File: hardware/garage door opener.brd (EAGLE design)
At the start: 50.8 x 40.6 mm, 26 parts, among them K1 HE3621, K2 HE3621

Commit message: Updated with BOM
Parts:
- C1, C2: value (none) -> 10uf
- D1, D2: value (none) -> 1N4004
- R1, R3: value (none) -> 20
- R2, R4: value 2.3k -> 4k
- R5, R6: value (none) -> 1k
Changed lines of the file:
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@@
 </autorouter>
 <elements>
-<element name="T1" library="transistor-neu-to92" package="SOT23-BEC" value="" x="21.59" y="5.08"/>
+<element name="T1" library="transistor-neu-to92" package="SOT23-BEC" value="" x="21.59" y="5.08">
+<attribute name="MPN" value="MMBT2222A" x="21.59" y="5.08" size="1.778" layer="27" display="off"/>
+</element>
 <element name="K1" library="relay" package="HE3621" value="HE3621" x="40.64" y="10.16" rot="R90">
 <attribute name="OC_NEWARK" value="50F7993" x="40.64" y="10.16" size="1.778" layer="27" rot="R90" display="off"/>
@@
 <element name="JP2" library="pinhead" package="1X15" value="" x="12.7" y="20.32" rot="R270"/>
 <element name="JP3" library="pinhead" package="1X15" value="" x="35.56" y="20.32" rot="R270"/>
-<element name="OPEN1" library="adafruit" package="1X2-3.5MM" value="1X2-3.5MM" x="48.26" y="8.89" rot="R90"/>
-<element name="SENS1" library="adafruit" package="1X2-3.5MM" value="1X2-3.5MM" x="48.26" y="16.51" rot="R90"/>
-<element name="R1" library="resistor" package="R0603" value="" x="44.45" y="2.54" rot="R270"/>
-<element name="R2" library="resistor" package="R0603" value="2.3k" x="17.78" y="5.08" rot="R270"/>
-<element name="D1" library="diode" package="DO214BA" value="" x="26.67" y="5.08" rot="R90"/>
-<element name="C1" library="resistor" package="C0603" value="" x="2.54" y="6.35"/>
-<element name="C2" library="resistor" package="C0603" value="" x="2.54" y="10.16"/>
+<element name="OPEN1" library="adafruit" package="1X2-3.5MM" value="1X2-3.5MM" x="48.26" y="8.89" rot="R90">
+<attribute name="MPN" value="OSTTE020161" x="48.26" y="8.89" size="1.778" layer="27" rot="R90" display="off"/>
+</element>
+<element name="SENS1" library="adafruit" package="1X2-3.5MM" value="1X2-3.5MM" x="48.26" y="16.51" rot="R90">
+<attribute name="MPN" value="OSTTE020161" x="48.26" y="16.51" size="1.778" layer="27" rot="R90" display="off"/>
+</element>
+<element name="R1" library="resistor" package="R0603" value="20" x="44.45" y="2.54" rot="R270"/>
+<element name="R2" library="resistor" package="R0603" value="4k" x="17.78" y="5.08" rot="R270"/>
+<element name="D1" library="diode" package="DO214BA" value="1N4004" x="26.67" y="5.08" rot="R90"/>
+<element name="C1" library="resistor" package="C0603" value="10uf" x="2.54" y="6.35"/>
+<element name="C2" library="resistor" package="C0603" value="10uf" x="2.54" y="10.16"/>
 <element name="LED1" library="resistor" package="R0603" value="" x="1.905" y="33.02" rot="R90"/>
 <element name="LED2" library="resistor" package="R0603" value="" x="1.905" y="26.67" rot="R90"/>
-<element name="SENS2" library="adafruit" package="1X2-3.5MM" value="1X2-3.5MM" x="48.26" y="31.75" rot="R90"/>
-<element name="R3" library="resistor" package="R0603" value="" x="44.45" y="38.1" rot="R270"/>
+<element name="SENS2" library="adafruit" package="1X2-3.5MM" value="1X2-3.5MM" x="48.26" y="31.75" rot="R90">
+<attribute name="MPN" value="OSTTE020161" x="48.26" y="31.75" size="1.778" layer="27" rot="R90" display="off"/>
+</element>
+<element name="R3" library="resistor" package="R0603" value="20" x="44.45" y="38.1" rot="R270"/>
 <element name="K2" library="relay" package="HE3621" value="HE3621" x="40.64" y="30.48" rot="R90">
 <attribute name="OC_NEWARK" value="50F7993" x="40.64" y="30.48" size="1.778" layer="27" rot="R90" display="off"/>
@@
 <attribute name="OC_FARNELL" value="9561943" x="40.64" y="30.48" size="1.778" layer="27" rot="R90" display="off"/>
 </element>
-<element name="OPEN2" library="adafruit" package="1X2-3.5MM" value="1X2-3.5MM" x="48.26" y="24.13" rot="R90"/>
-<element name="T2" library="transistor-neu-to92" package="SOT23-BEC" value="" x="21.59" y="29.21"/>
-<element name="D2" library="diode" package="DO214BA" value="" x="26.67" y="29.21" rot="R90"/>
-<element name="R4" library="resistor" package="R0603" value="2.3k" x="17.78" y="29.21" rot="R270"/>
+<element name="OPEN2" library="adafruit" package="1X2-3.5MM" value="1X2-3.5MM" x="48.26" y="24.13" rot="R90">
+<attribute name="MPN" value="OSTTE020161" x="48.26" y="24.13" size="1.778" layer="27" rot="R90" display="off"/>
+</element>
+<element name="T2" library="transistor-neu-to92" package="SOT23-BEC" value="" x="21.59" y="29.21">
+<attribute name="MPN" value="MMBT2222A" x="21.59" y="29.21" size="1.778" layer="27" display="off"/>
+</element>
+<element name="D2" library="diode" package="DO214BA" value="1N4004" x="26.67" y="29.21" rot="R90"/>
+<element name="R4" library="resistor" package="R0603" value="4k" x="17.78" y="29.21" rot="R270"/>
 <element name="JP4" library="pinhead" package="1X03" value="" x="2.54" y="20.32" rot="R270"/>
 <element name="D3" library="diode" package="DO41-10" value="1N4004" x="30.48" y="7.62" rot="R90"/>
 <element name="D4" library="diode" package="DO41-10" value="1N4004" x="30.48" y="31.75" rot="R90"/>
-<element name="R5" library="resistor" package="R0603" value="" x="4.445" y="33.02" rot="R270"/>
-<element name="R6" library="resistor" package="R0603" value="" x="4.445" y="26.67" rot="R270"/>
+<element name="R5" library="resistor" package="R0603" value="1k" x="4.445" y="33.02" rot="R270"/>
+<element name="R6" library="resistor" package="R0603" value="1k" x="4.445" y="26.67" rot="R270"/>
 </elements>
 <signals>

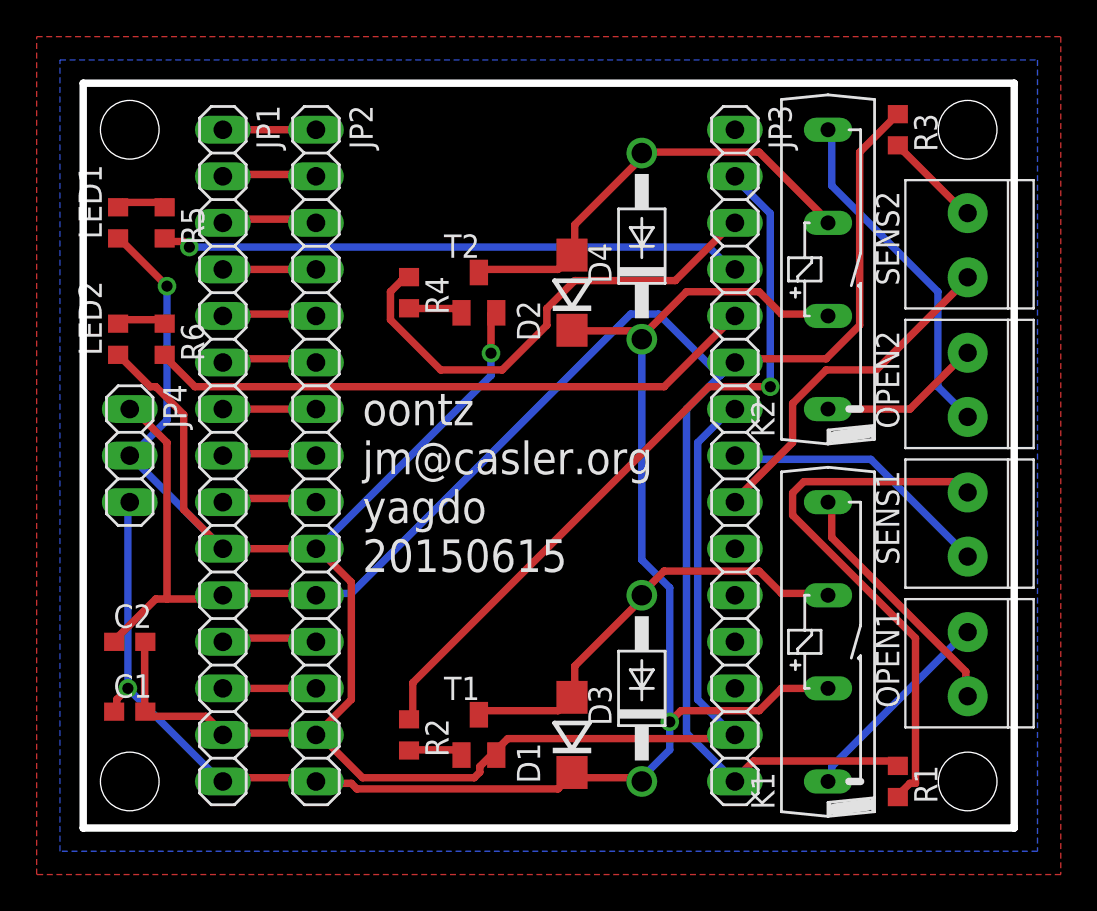
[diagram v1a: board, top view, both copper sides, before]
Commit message: Updated with pull down resistor for sense inputs.
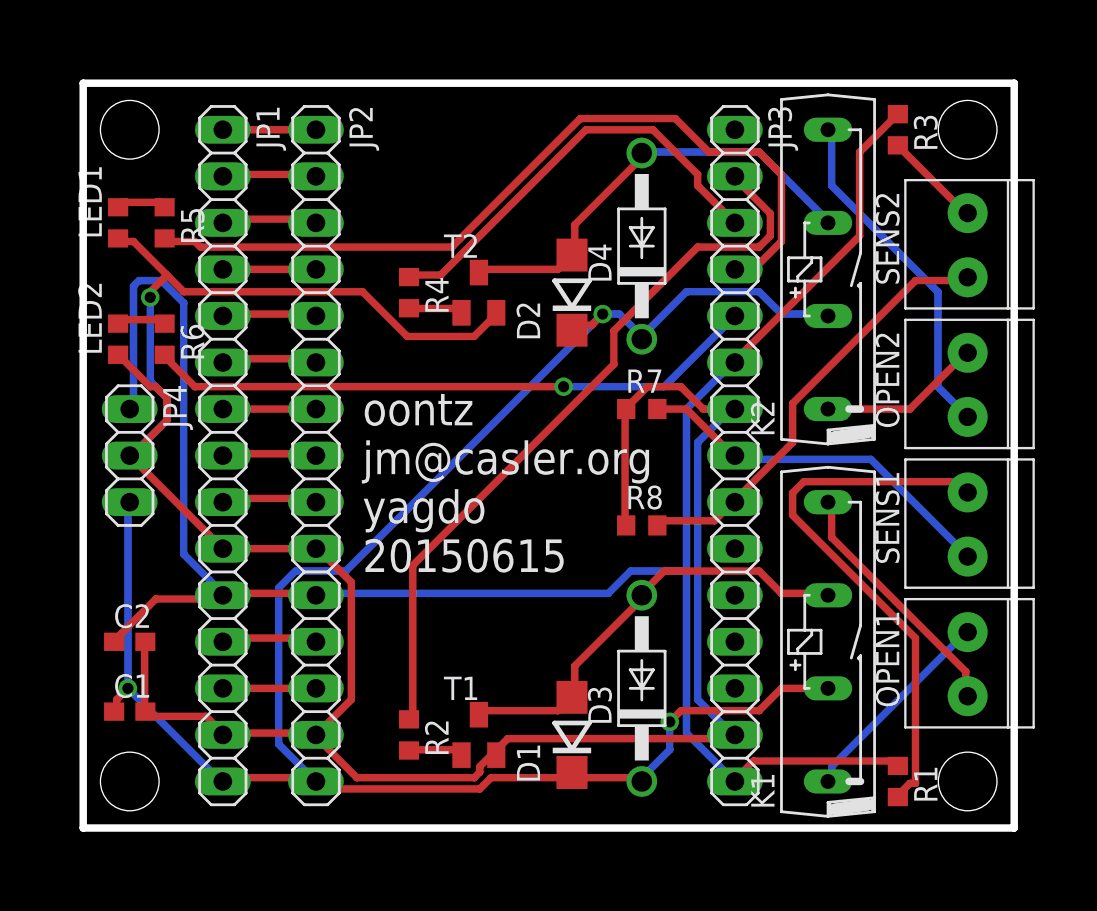
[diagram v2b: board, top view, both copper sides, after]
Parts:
- added R7, R8: 10k, resistor:R0603
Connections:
- net GND: now also R7.1, R8.1
- net N$14: now also R7.2
- net N$22: now also R8.2
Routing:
- net +5V: track 94.0 -> 108.5 mm, vias 2 -> 3
- net N$19: track 31.8 -> 44.9 mm, vias 1 -> 0
- net GND: track 126.6 -> 138.6 mm, vias 2 -> 1
- net N$14: track 15.0 -> 20.3 mm
- net N$22: track 19.1 -> 23.9 mm
- net N$26: track 26.7 -> 23.6 mm
- net +3V3: track 109.2 -> 112.0 mm
- net N$20: vias 0 -> 1
- net N$17: vias 1 -> 0
- removed copper zone on layer 1, net GND
- removed copper zone on layer 16, net GND

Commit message: Removed trough hole diode, removed top silkscreen, rerouted.
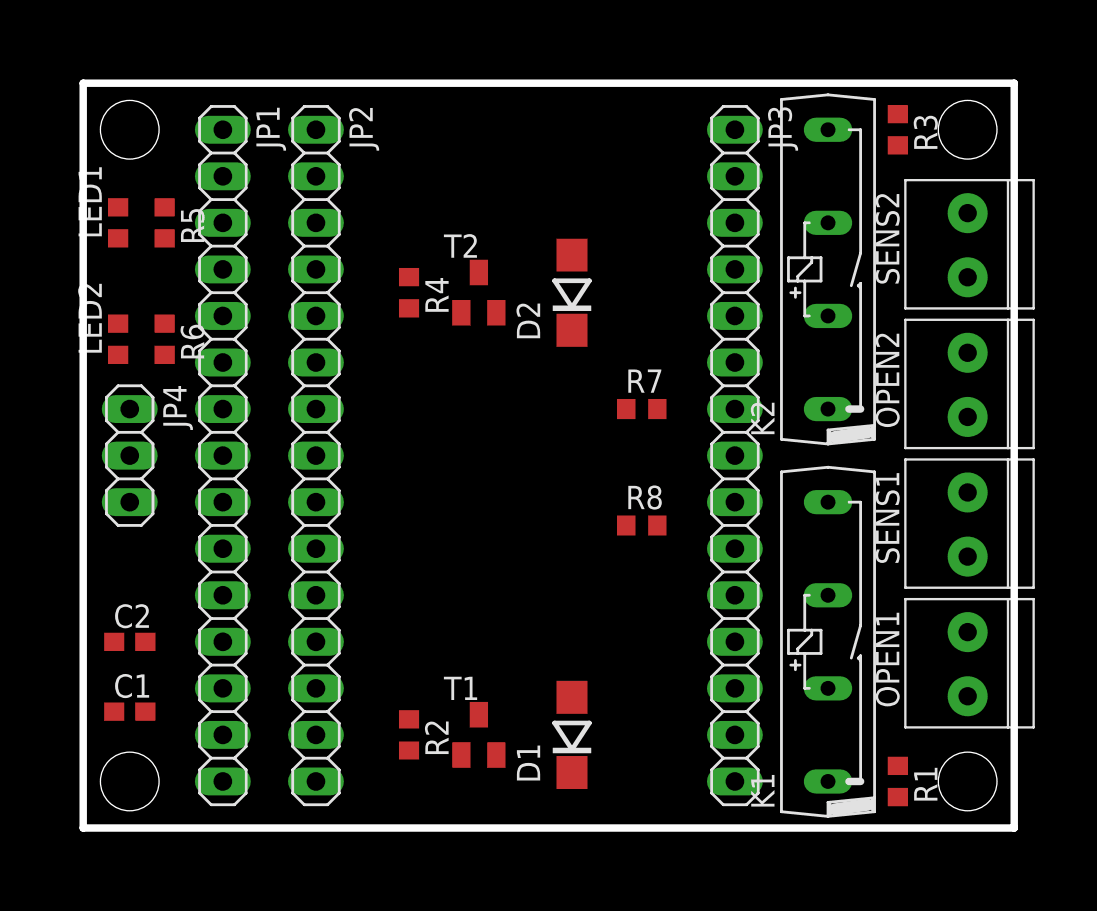
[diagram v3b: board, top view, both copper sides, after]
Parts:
- removed D3, D4: 1N4004, diode:DO41-10
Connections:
- net +5V: no longer D3.C, D4.C
- net N$16: no longer D3.A
- net N$25: no longer D4.A
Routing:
- net GND: track 138.6 -> 0.00 mm, vias 1 -> 0
- net +3V3: track 112.0 -> 0.00 mm
- net +5V: track 108.5 -> 0.00 mm, vias 3 -> 0
- net N$19: track 44.9 -> 0.00 mm
- net N$17: track 40.6 -> 0.00 mm
- net N$20: track 33.5 -> 0.00 mm, vias 1 -> 0
- net N$15: track 30.1 -> 0.00 mm
- net N$25: track 24.5 -> 0.00 mm
- net N$16: track 24.0 -> 0.00 mm
- net N$22: track 23.9 -> 0.00 mm
- net N$26: track 23.6 -> 0.00 mm
- net N$14: track 20.3 -> 0.00 mm
- net N$24: track 18.9 -> 0.00 mm
- net N$11: track 13.8 -> 0.00 mm
- net N$10: track 11.3 -> 0.00 mm
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
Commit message: removed through hole diode
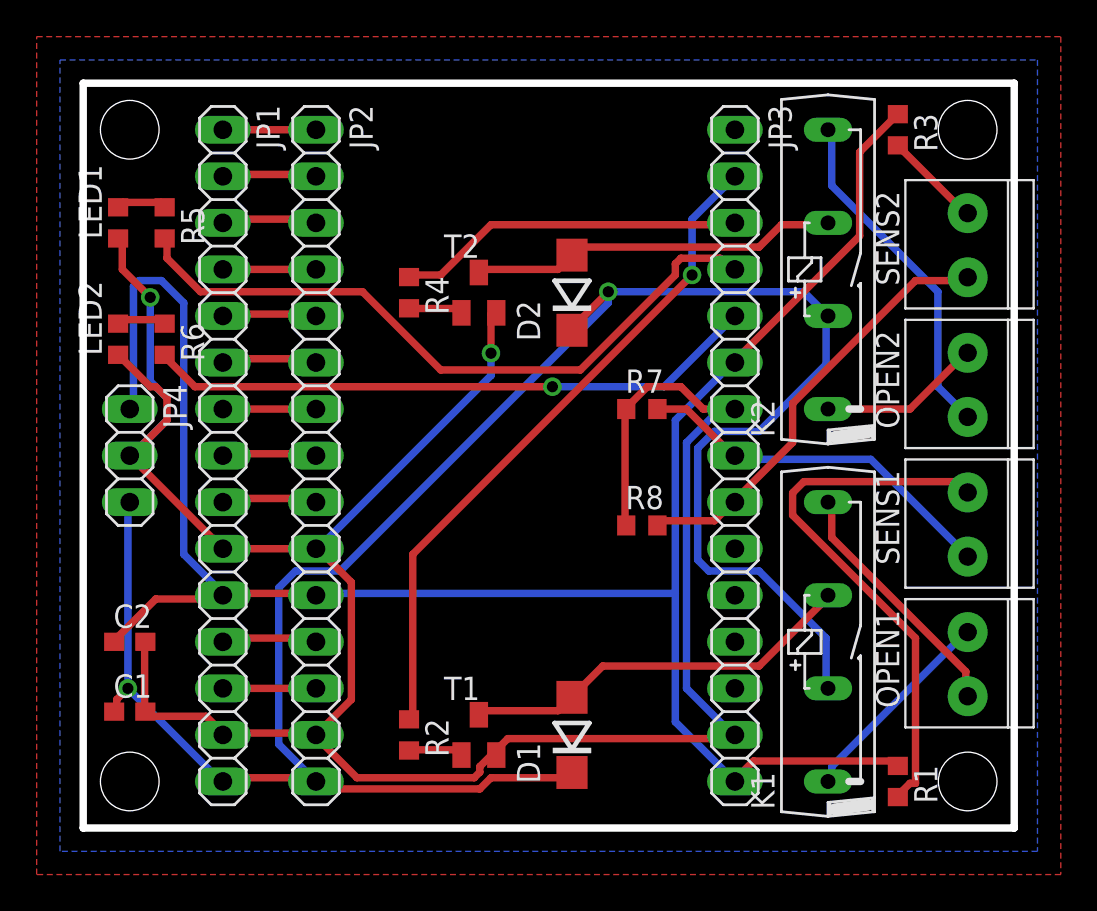
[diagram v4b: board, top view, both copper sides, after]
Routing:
- net GND: track 0.00 -> 135.5 mm, vias 0 -> 2
- net +5V: track 0.00 -> 120.3 mm, vias 0 -> 2
- net +3V3: track 0.00 -> 111.4 mm
- net N$19: track 0.00 -> 37.8 mm
- net N$17: track 0.00 -> 37.0 mm, vias 0 -> 1
- net N$20: track 0.00 -> 33.5 mm, vias 0 -> 1
- net N$15: track 0.00 -> 30.1 mm
- net N$22: track 0.00 -> 23.9 mm
- net N$16: track 0.00 -> 21.9 mm
- net N$14: track 0.00 -> 20.3 mm
- net N$25: track 0.00 -> 20.2 mm
- net N$26: track 0.00 -> 19.0 mm
- net N$24: track 0.00 -> 18.9 mm
- net N$11: track 0.00 -> 13.8 mm
- net N$10: track 0.00 -> 11.3 mm
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- added copper zone on layer 1, net GND
- added copper zone on layer 16, net GND
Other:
- board text added: "yado oontz jm@casler.org 20150627"
- board text removed: "oontz jm@casler.org yagdo 20150615"

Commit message: Removed power pads from left (not really needed?). Replaced LEDs with a proper LED footprint. Moved capacitors closer to headers.
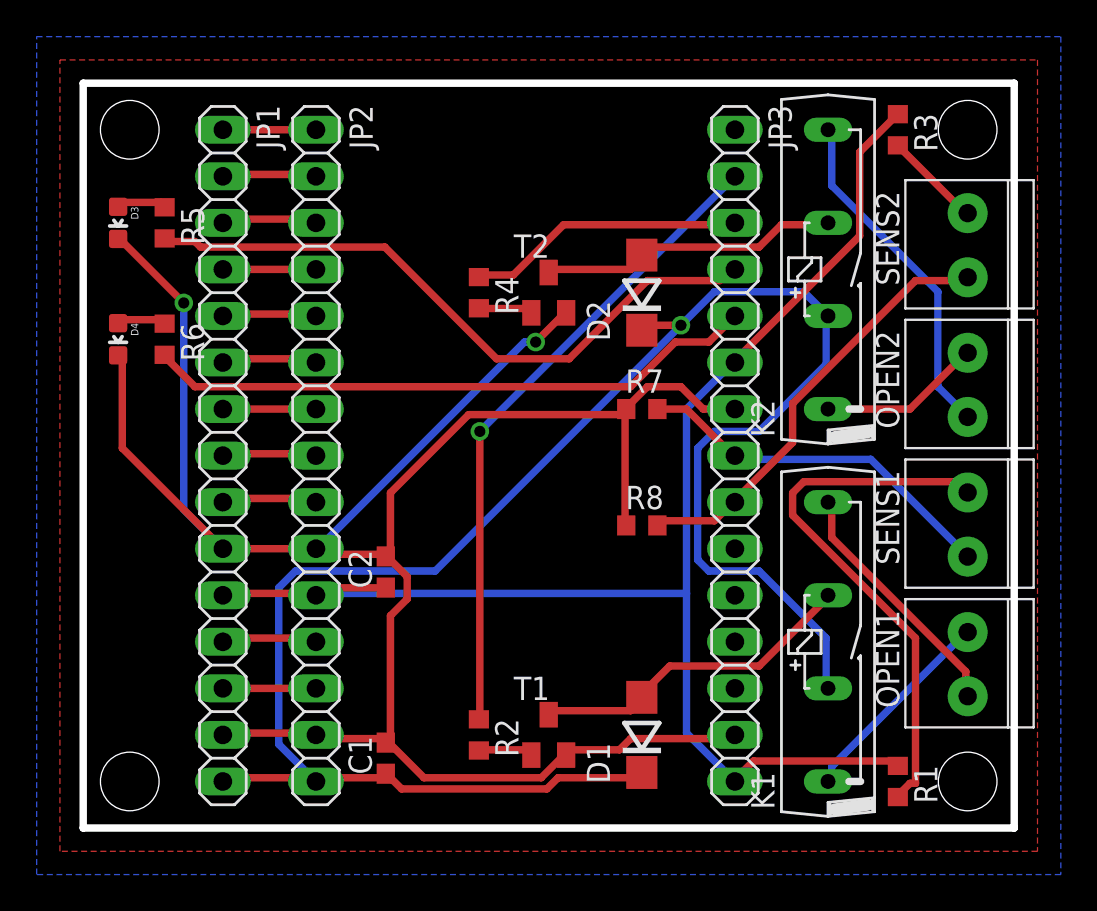
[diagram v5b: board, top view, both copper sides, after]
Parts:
- removed JP4: (no value), pinhead:1X03
- removed LED1, LED2: (no value), resistor:R0603
- added D3, D4: (no value), SparkFun-LED:LED-0603
- moved C2 14.5 mm to (16.5, 14.0), turned to 90 degrees
- moved C1 14.2 mm to (16.5, 3.81), turned to 90 degrees
- moved D1 3.81 mm to (30.5, 5.08)
- moved D2 3.81 mm to (30.5, 29.2)
- moved R2 3.81 mm to (21.6, 5.08)
- moved R4 3.81 mm to (21.6, 29.2)
- moved T1 3.81 mm to (25.4, 5.08)
- moved T2 3.81 mm to (25.4, 29.2)
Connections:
- net +3V3: no longer JP4.1
- net +5V: no longer JP4.3
- net GND: now also D3.C, D4.C; no longer JP4.2, LED1.1, LED2.1
- net N$28: now also D4.A; no longer LED2.2
- net N$29: now also D3.A; no longer LED1.2
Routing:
- net +3V3: track 111.4 -> 81.3 mm
- net +5V: track 120.3 -> 104.6 mm, vias 2 -> 1
- net N$26: track 19.0 -> 15.2 mm
- net N$16: track 21.9 -> 18.2 mm
- net N$25: track 20.2 -> 16.5 mm
- net GND: track 135.5 -> 133.5 mm
- net N$19: track 37.8 -> 35.9 mm
- net N$17: track 37.0 -> 35.4 mm
- net N$20: vias 1 -> 0

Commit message: Updated with footprint for ds18b20 ... why? feature creep!
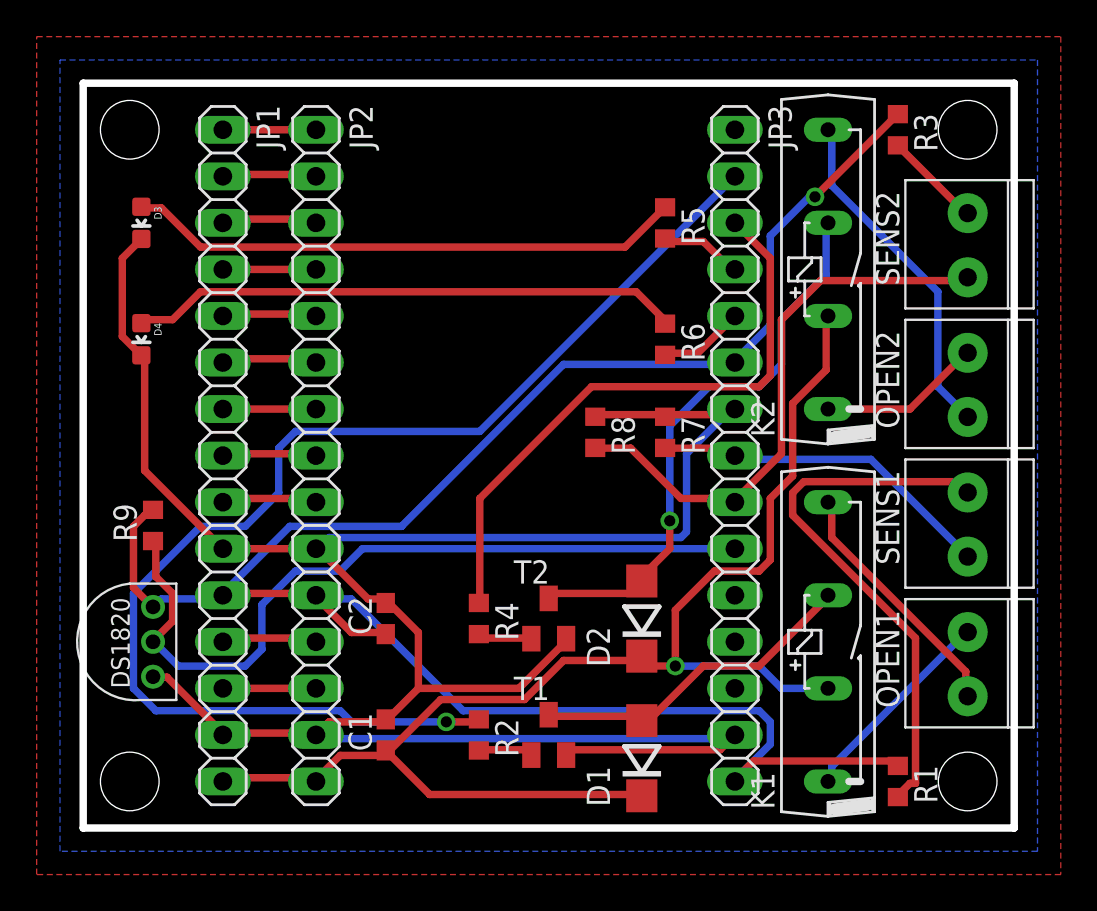
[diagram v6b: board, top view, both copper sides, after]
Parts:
- added DS18B20: DS18B20TO92, Ava:DS1820
- added R9: 4k, resistor:R0603
- moved R5 27.3 mm to (31.8, 33.0)
- moved R6 27.3 mm to (31.8, 26.7)
- moved D2 17.8 mm to (30.5, 11.4)
- moved R4 17.8 mm to (21.6, 11.4)
- moved T2 17.8 mm to (25.4, 11.4)
- moved R8 5.68 mm to (27.9, 21.6), turned to 270 degrees
- moved C2 2.54 mm to (16.5, 11.4)
- moved R7 1.80 mm to (31.8, 21.6), turned to 270 degrees
- moved C1 1.27 mm to (16.5, 5.08)
- moved D1 1.27 mm to (30.5, 3.81)
- moved D3 1.27 mm to (3.17, 33.0)
- moved D4 1.27 mm to (3.17, 26.7)
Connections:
- new net N$30: DS18B20.DQ, JP3.10, R9.1
- net +3V3: now also DS18B20.VDD, R9.2
- net GND: now also DS18B20.GND
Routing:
- net N$30: track 0.00 -> 42.7 mm
- net N$17: track 35.4 -> 68.5 mm
- net N$19: track 35.9 -> 4.49 mm
- net +3V3: track 81.3 -> 112.3 mm, vias 0 -> 1
- net N$20: track 33.5 -> 4.67 mm
- net +5V: track 104.6 -> 76.0 mm
- net N$29: track 2.79 -> 30.4 mm
- net N$28: track 2.71 -> 30.1 mm
- net N$26: track 15.2 -> 33.5 mm
- net N$25: track 16.5 -> 30.9 mm, vias 0 -> 1
- net N$22: track 23.9 -> 31.0 mm
- net GND: track 133.5 -> 130.6 mm, vias 2 -> 0
- net N$14: track 20.3 -> 19.0 mm
